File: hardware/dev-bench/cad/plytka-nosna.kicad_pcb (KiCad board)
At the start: 2 copper layers, 170 x 100 mm, 74 parts, among them J1 ARDUINO POWER, J10 CC1120EM P2, J11 ANALIZATOR, J12 VTEST 0-15V, J2 ARDUINO A0-A5, J3 ARDUINO D0-D7, J4 ARDUINO D8-SCL, J5 DEVKITC J1, J6 DEVKITC J3, J7 SHARP LS027B7DH01A, J9 CC1120EM P1, Q1 MMBT3904, SW1 GÓRA, SW2 DÓŁ, SW3 OK, SW4 WSTECZ, SW5 CISZA, SW6 PRZYGOTOWANIE, U1 CY15B104QN-50SXI, U2 MCP1640, U3 TPS3840PH27, U4 74LVC1G32

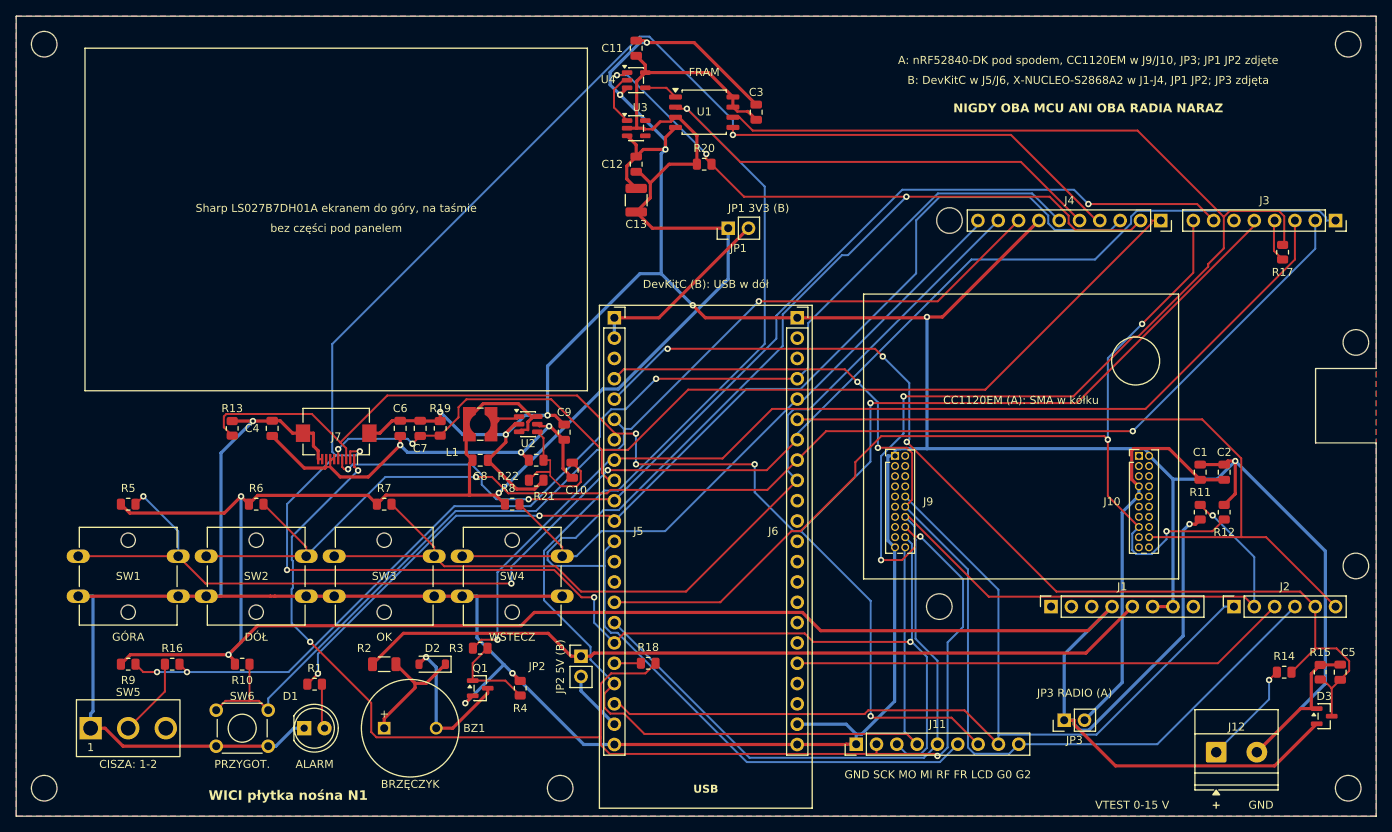
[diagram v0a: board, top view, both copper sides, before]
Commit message: N1.1: złącze panelu J7 odsunięte na zmierzoną taśmę FPC (F118)
Czoło J7 leży 9,4 mm od krawędzi szkła zamiast 2,3 mm. Wartość pochodzi
z pomiaru na pierwszym L0 (szkło 7,0-7,2 mm za obrysem przy czole 2,3 mm).
Katalog Hirose FH12 podaje koniec taśmy (3,1) mm za czołem, co dawałoby
10,4 mm; dłuższy odstęp przesuwa szkło w stronę krawędzi płytki (4 mm
miejsca), a pas 1 mm pod obrysem panelu jest wolny od części (FPC_TOL,
asercja w make_board.py).

Razem z J7 przesunięte R13, R19, C4, C6, C7; rząd R5-R8 na y 62 mm,
SW1-SW4, R3 i JP2 niżej. Płytka poprowadzona od nowa (Freerouting 2.5.0,
Java 25, 0 niepoprowadzonych), ERC 0, DRC 0 z kanarkiem reguł,
odtworzenie w osobnej kopii bez różnic. Paczka fabrication/N1/ i wydruk
1:1 wyeksportowane, napis i rewizja N1.1. Dokumenty: plytka-nosna,
uruchomienie (krok 7 dla obu rewizji), przed-produkcja, F118, zapisy
odtworzenia i przymiarki; test obudowy z nowym położeniem przycisków.
Przymiarka 1:1 N1.1 pozostaje otwarta.

Co-Authored-By: Claude Opus 5.5 <noreply@anthropic.com>
Signed-off-by: Tomek Mierzwa <16899265+tmierzwa@users.noreply.github.com>
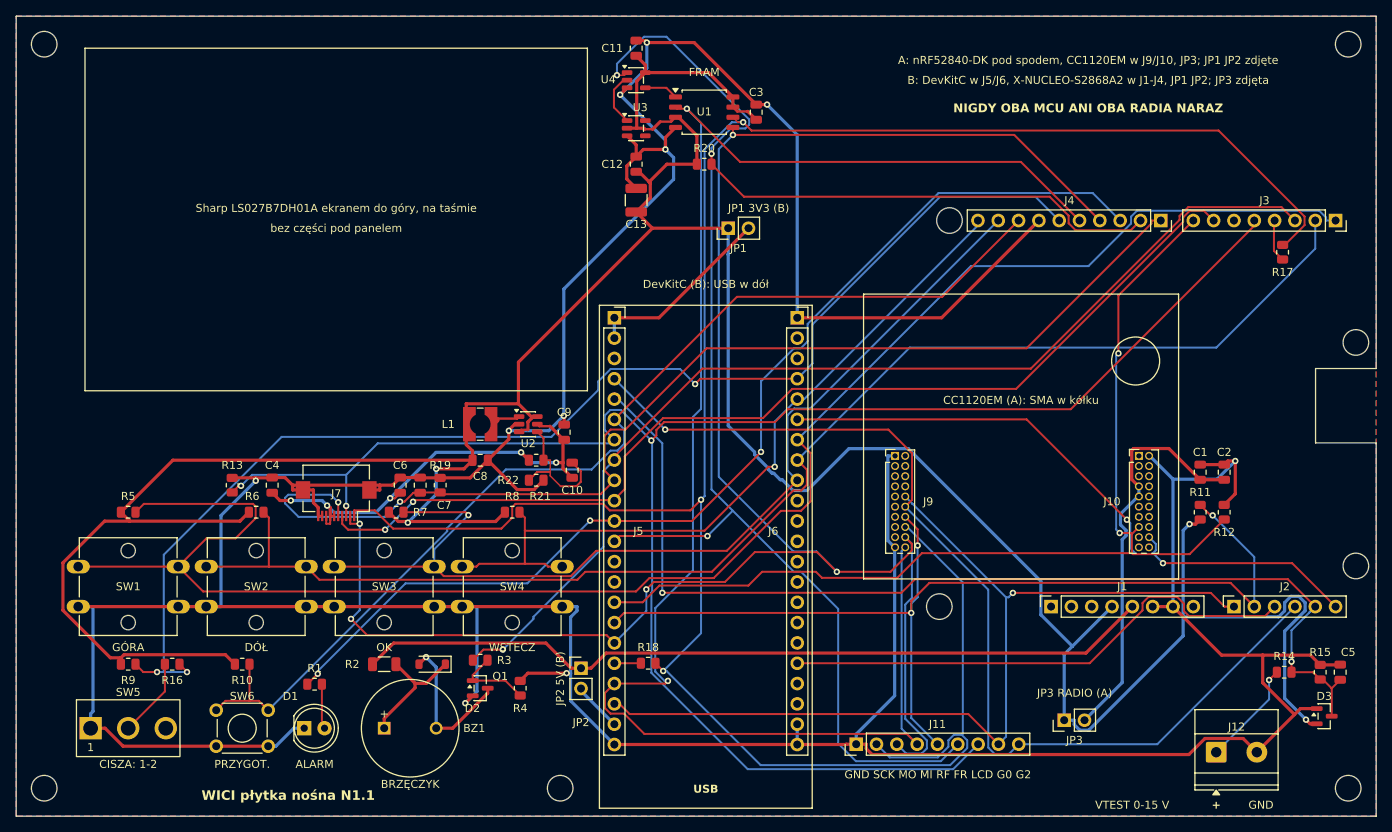
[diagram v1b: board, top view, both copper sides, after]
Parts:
- moved C4 7.10 mm to (62.0, 88.6)
- moved C6 7.10 mm to (78.0, 88.6)
- moved C7 7.10 mm to (80.5, 88.6)
- moved J7 7.10 mm to (70.0, 90.6)
- moved R13 7.10 mm to (57.0, 88.6)
- moved R19 7.10 mm to (83.0, 88.6)
- moved R7 1.80 mm to (77.5, 92.0)
- moved JP2 1.50 mm to (100.6, 111.5)
- moved R3 1.50 mm to (88.0, 110.5)
- moved SW1 1.30 mm to (37.8, 98.8)
- moved SW2 1.30 mm to (53.8, 98.8)
- moved SW3 1.30 mm to (69.8, 98.8)
- moved SW4 1.30 mm to (85.8, 98.8)
- moved R5 1.00 mm to (44.0, 92.0)
- moved R6 1.00 mm to (60.0, 92.0)
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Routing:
- net /SPI_MOSI: track 276.5 -> 243.4 mm
- net /SPI_SCK: track 321.9 -> 292.2 mm, vias 6 -> 3
- net /BTN_UP: track 191.5 -> 215.5 mm, vias 3 -> 0
- net /LCD_CS: track 212.5 -> 230.7 mm, vias 5 -> 3
- net /LCD_DISP: track 127.5 -> 140.5 mm
- net /RF_GPIO3: track 94.3 -> 81.4 mm, vias 0 -> 2
- net /SW_CISZA: track 147.9 -> 159.6 mm
- net /RF_CS: track 142.1 -> 130.6 mm, vias 1 -> 3
- net /GND: track 612.4 -> 602.7 mm, vias 12 -> 10
- net /SPI_MISO: track 218.2 -> 208.8 mm, vias 1 -> 2
- net /FRAM_CS: track 213.5 -> 205.7 mm
- net /RF_GPIO0: track 122.3 -> 116.1 mm, vias 0 -> 1
- net /RF_GPIO2: track 134.6 -> 128.8 mm, vias 2 -> 1
- net /BTN_OK: track 119.2 -> 124.9 mm, vias 0 -> 1
- net /BTN_BACK: track 90.9 -> 95.9 mm, vias 0 -> 1
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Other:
- board text added: "WICI płytka nośna N1.1"
- board text removed: "WICI płytka nośna N1"
